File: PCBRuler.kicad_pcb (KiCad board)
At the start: 2 copper layers, 156.7 x 25.4 mm, 24 parts

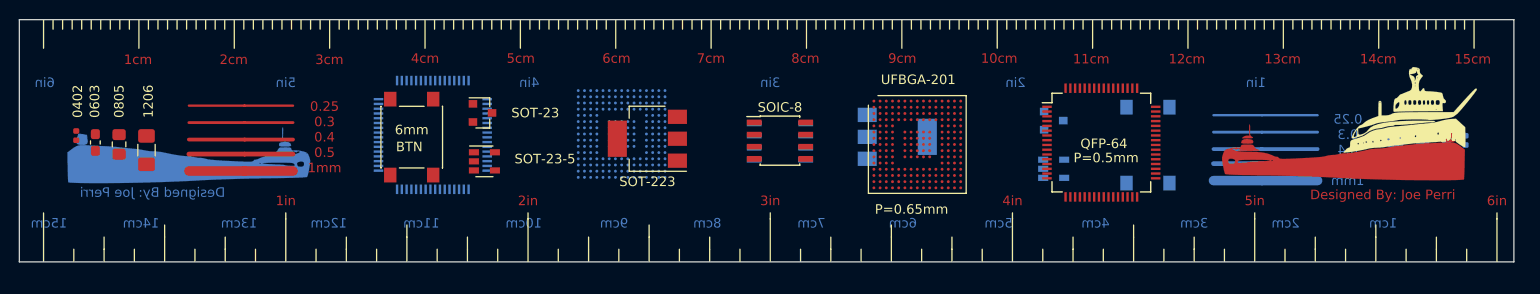
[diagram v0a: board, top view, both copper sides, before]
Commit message: Slightly round corners
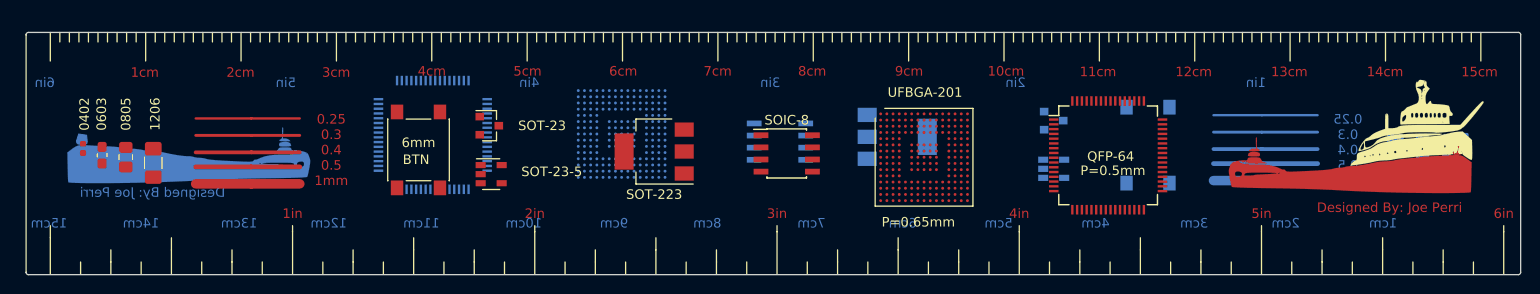
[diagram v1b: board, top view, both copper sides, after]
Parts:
- moved 0402 1.52 mm to (152.2, 126.9)
- moved 0603 1.52 mm to (154.2, 127.6)
- moved SOT-23-5 1.52 mm to (195.0, 129.6)
- moved UFBGA-201 1.52 mm to (240.4, 127.8)
- moved 0805 1.52 mm to (156.7, 127.8)
- moved 6mm 1.52 mm to (187.4, 127.1)
- moved SOT-223 1.52 mm to (212.1, 127.2)
- moved G*** 1.52 mm to (285.7, 125.6)
- moved QFP-64 1.52 mm to (259.7, 127.6)
- moved SOIC-8 1.52 mm to (226.0, 127.4)
- moved SOT-23 1.52 mm to (194.8, 124.5)
- moved 1206 1.52 mm to (159.6, 128.4)
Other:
- outline, holes or cut-outs redrawn

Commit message: Fix mark alignment
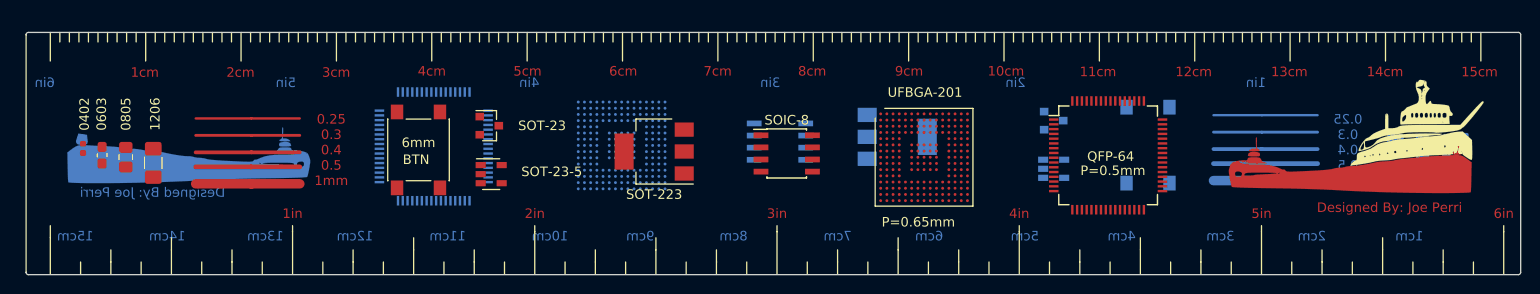
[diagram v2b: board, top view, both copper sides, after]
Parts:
- moved QFP-64 1.20 mm to (189.0, 126.7), turned to 180 degrees
- moved UFBGA-201 1.20 mm to (208.7, 126.6), turned to 90 degrees
